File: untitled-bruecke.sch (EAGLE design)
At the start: 16 parts, among them U1 C-TEENSY++

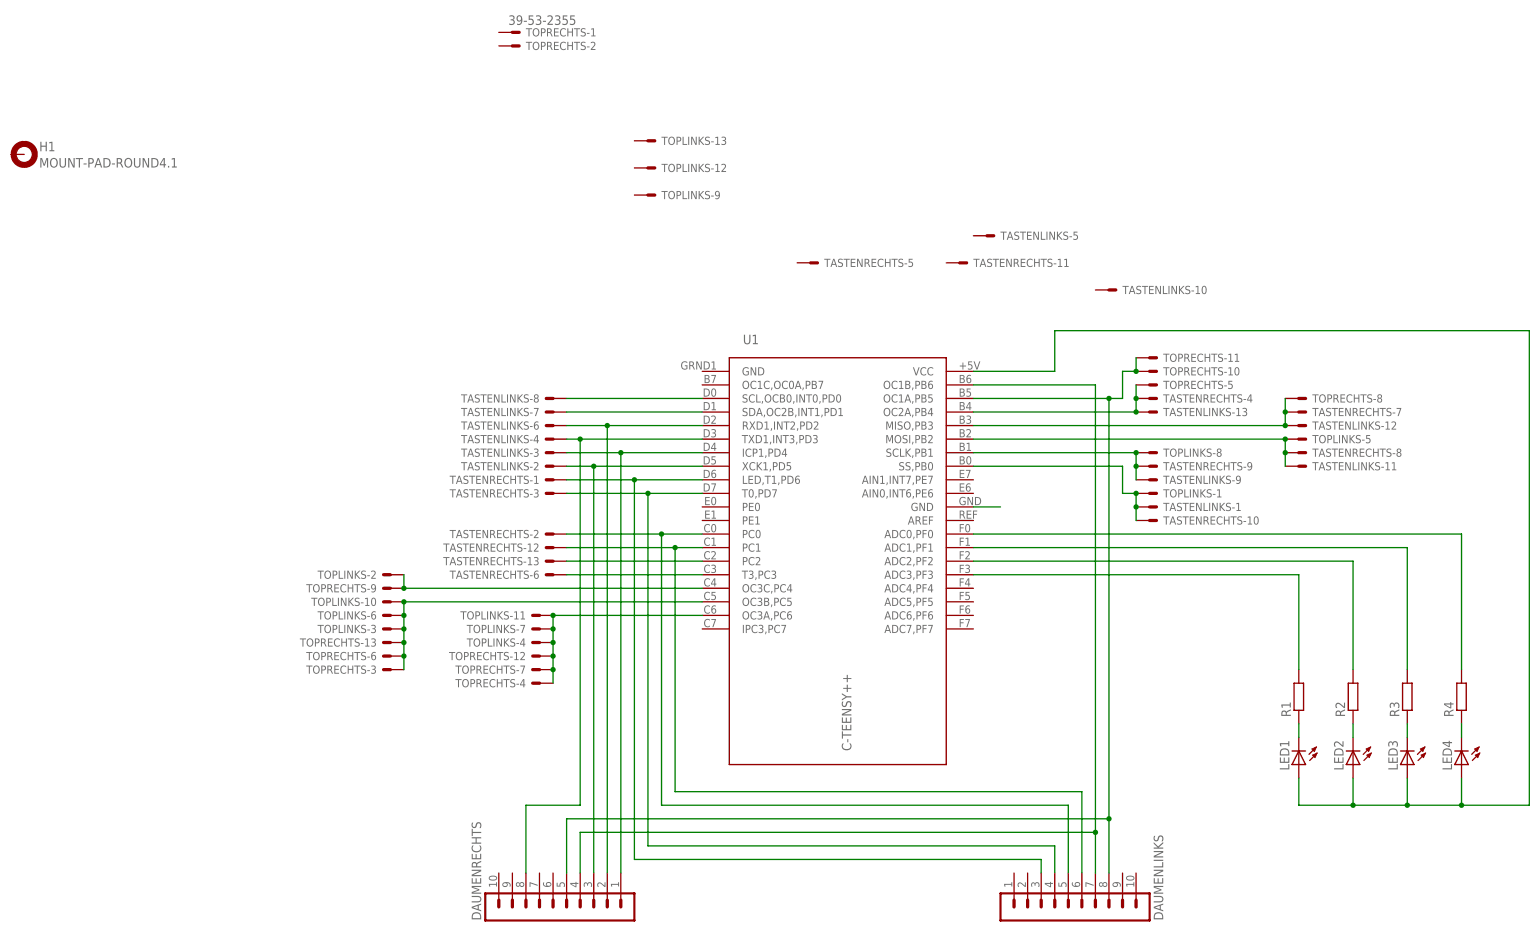
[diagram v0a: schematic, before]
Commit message: Turn board and schematic into new revision: “kinX”
The new controller revision uses a Teensy 3.6, which requires some rewiring.

I used the chance to perform a bunch of cleanups:

• Use SMD LEDs instead of THT (resistors were already SMD)
• Move LED silkscreen labels to the correct side
• Correct the names of all connectors to match the kinesis PCBs
• Change the matrix to be easier to wire up
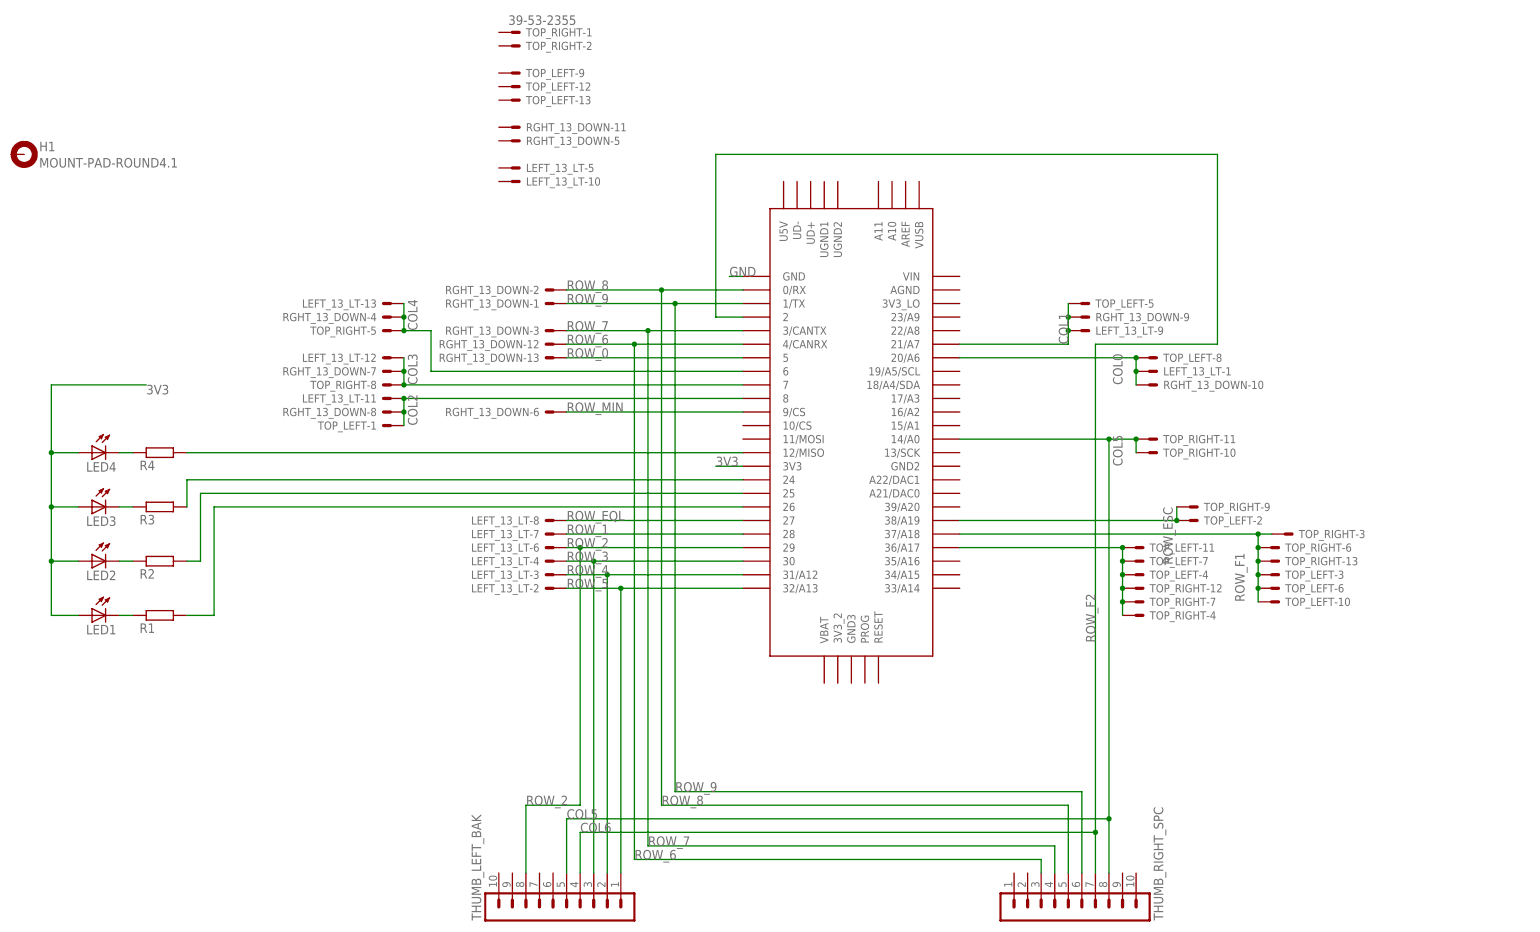
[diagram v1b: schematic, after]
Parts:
- removed TASTENLINKS, TASTENRECHTS, TOPLINKS: 39-53-2355, con-molex-39-53:39-53-2355
- added LEFT_13_LT, RGHT_13_DOWN, TOP_LEFT: 39-53-2355, con-molex-39-53:39-53-2355
- LED1, LED2, LED3, LED4: device led:LED3MM -> led:LEDSML1206
- U1: value C-TEENSY++ -> TEENSY_3.5/3.6; device teensypp:C-TEENSY++ -> Teensy356:TEENSY_3.5/3.6
- renumbered DAUMENLINKS to THUMB_RIGHT_SPC, DAUMENRECHTS to THUMB_LEFT_BAK, TOPRECHTS to TOP_RIGHT
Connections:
- removed net B0: TASTENLINKS-1.S, TASTENRECHTS-10.S, TOPLINKS-1.S, U1.SS,PB0
- removed net B1: TASTENLINKS-9.S, TASTENRECHTS-9.S, TOPLINKS-8.S, U1.SCLK,PB1
- removed net B2: TASTENLINKS-11.S, TASTENRECHTS-8.S, TOPLINKS-5.S, U1.MOSI,PB2
- removed net B3: TASTENLINKS-12.S, TASTENRECHTS-7.S, TOP_RIGHT-8.S, U1.MISO,PB3
- removed net B4: TASTENLINKS-13.S, TASTENRECHTS-4.S, TOP_RIGHT-5.S, U1.OC2A,PB4
- removed net B5: THUMB_LEFT_BAK.5, THUMB_RIGHT_SPC.8, TOP_RIGHT-10.S, TOP_RIGHT-11.S, U1.OC1A,PB5
- removed net B6: THUMB_LEFT_BAK.4, THUMB_RIGHT_SPC.7, U1.OC1B,PB6
- removed net C0: TASTENRECHTS-2.S, THUMB_RIGHT_SPC.5, U1.PC0
- removed net C1: TASTENRECHTS-12.S, THUMB_RIGHT_SPC.6, U1.PC1
- removed net C2: TASTENRECHTS-13.S, U1.PC2
- removed net C3: TASTENRECHTS-6.S, U1.T3,PC3
- removed net C4: TOPLINKS-2.S, TOP_RIGHT-9.S, U1.OC3C,PC4
- removed net C5: TOPLINKS-10.S, TOPLINKS-3.S, TOPLINKS-6.S, TOP_RIGHT-13.S, TOP_RIGHT-3.S, TOP_RIGHT-6.S, U1.OC3B,PC5
- removed net C6: TOPLINKS-11.S, TOPLINKS-4.S, TOPLINKS-7.S, TOP_RIGHT-12.S, TOP_RIGHT-4.S, TOP_RIGHT-7.S, U1.OC3A,PC6
- removed net D0: TASTENLINKS-8.S, U1.SCL,OCB0,INT0,PD0
- removed net D1: TASTENLINKS-7.S, U1.SDA,OC2B,INT1,PD1
- removed net D2: TASTENLINKS-6.S, THUMB_LEFT_BAK.2, U1.RXD1,INT2,PD2
- removed net D3: TASTENLINKS-4.S, THUMB_LEFT_BAK.8, U1.TXD1,INT3,PD3
- removed net D4: TASTENLINKS-3.S, THUMB_LEFT_BAK.1, U1.ICP1,PD4
- removed net D5: TASTENLINKS-2.S, THUMB_LEFT_BAK.3, U1.XCK1,PD5
- removed net D6: TASTENRECHTS-1.S, THUMB_RIGHT_SPC.3, U1.LED,T1,PD6
- removed net D7: TASTENRECHTS-3.S, THUMB_RIGHT_SPC.4, U1.T0,PD7
- removed net N$1: U1.GND@1
- removed net N$11: LED1.A, LED2.A, LED3.A, LED4.A, U1.VCC
- new net 3V3: LED1.A, LED2.A, LED3.A, LED4.A, U1.3V3
- new net COL0: LEFT_13_LT-1.S, RGHT_13_DOWN-10.S, TOP_LEFT-8.S, U1.20/A6
- new net COL1: LEFT_13_LT-9.S, RGHT_13_DOWN-9.S, TOP_LEFT-5.S, U1.21/A7
- new net COL2: LEFT_13_LT-11.S, RGHT_13_DOWN-8.S, TOP_LEFT-1.S, U1.8
- new net COL3: LEFT_13_LT-12.S, RGHT_13_DOWN-7.S, TOP_RIGHT-8.S, U1.7
- new net COL4: LEFT_13_LT-13.S, RGHT_13_DOWN-4.S, TOP_RIGHT-5.S, U1.6
- new net COL5: THUMB_LEFT_BAK.5, THUMB_RIGHT_SPC.8, TOP_RIGHT-10.S, TOP_RIGHT-11.S, U1.14/A0
- new net COL6: THUMB_LEFT_BAK.4, THUMB_RIGHT_SPC.7, U1.2
- new net GND: U1.GND
- new net ROW_0: RGHT_13_DOWN-13.S, U1.5
- new net ROW_1: LEFT_13_LT-7.S, U1.28
- new net ROW_2: LEFT_13_LT-6.S, THUMB_LEFT_BAK.8, U1.29
- new net ROW_3: LEFT_13_LT-4.S, THUMB_LEFT_BAK.3, U1.30
- new net ROW_4: LEFT_13_LT-3.S, THUMB_LEFT_BAK.2, U1.31/A12
- new net ROW_5: LEFT_13_LT-2.S, THUMB_LEFT_BAK.1, U1.32/A13
- new net ROW_6: RGHT_13_DOWN-12.S, THUMB_RIGHT_SPC.3, U1.4/CANRX
- new net ROW_7: RGHT_13_DOWN-3.S, THUMB_RIGHT_SPC.4, U1.3/CANTX
- new net ROW_8: RGHT_13_DOWN-2.S, THUMB_RIGHT_SPC.5, U1.0/RX
- new net ROW_9: RGHT_13_DOWN-1.S, THUMB_RIGHT_SPC.6, U1.1/TX
- new net ROW_EQL: LEFT_13_LT-8.S, U1.27
- new net ROW_ESC: TOP_LEFT-2.S, TOP_RIGHT-9.S, U1.38/A19
- new net ROW_F1: TOP_LEFT-10.S, TOP_LEFT-3.S, TOP_LEFT-6.S, TOP_RIGHT-13.S, TOP_RIGHT-3.S, TOP_RIGHT-6.S, U1.37/A18
- new net ROW_F2: TOP_LEFT-11.S, TOP_LEFT-4.S, TOP_LEFT-7.S, TOP_RIGHT-12.S, TOP_RIGHT-4.S, TOP_RIGHT-7.S, U1.36/A17
- new net ROW_MIN: RGHT_13_DOWN-6.S, U1.9/CS
- net N$10: now also R1.2, U1.26; no longer R4.2, U1.ADC0,PF0
- net N$7: now also R4.2, U1.12/MISO; no longer R1.2, U1.ADC3,PF3
- net N$8: now also R3.2, U1.24; no longer R2.2, U1.ADC2,PF2
- net N$9: now also R2.2, U1.25; no longer R3.2, U1.ADC1,PF1
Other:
- moved on the sheet: LED1, LED2, LED3, LED4, R1, R2, R3, R4
